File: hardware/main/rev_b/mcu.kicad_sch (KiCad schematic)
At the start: 23 parts, among them J10 SWD, U10 RP2354B, Y1 12MHz ABM8-272-T3

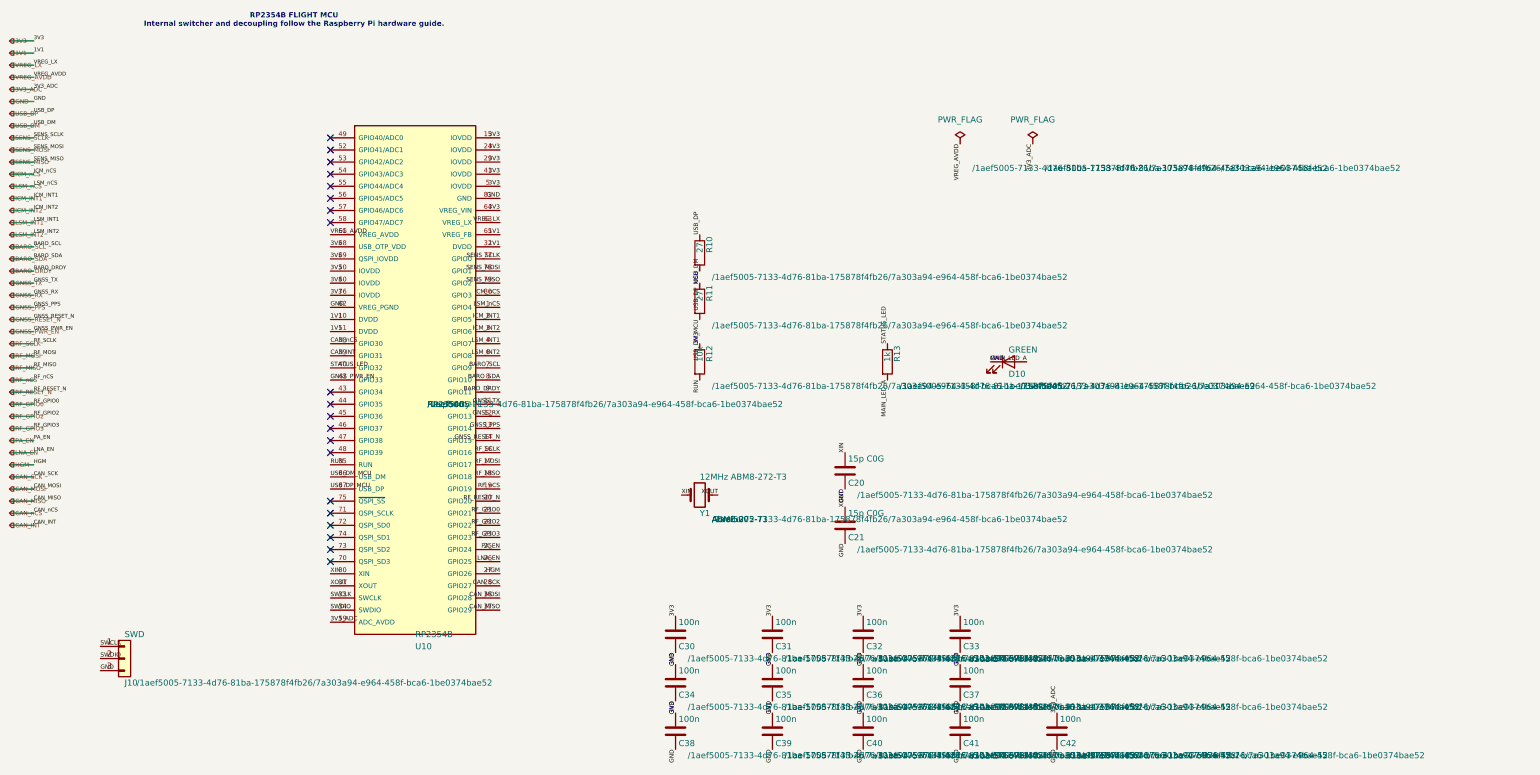
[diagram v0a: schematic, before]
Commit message: build: route and validate rev-b boards
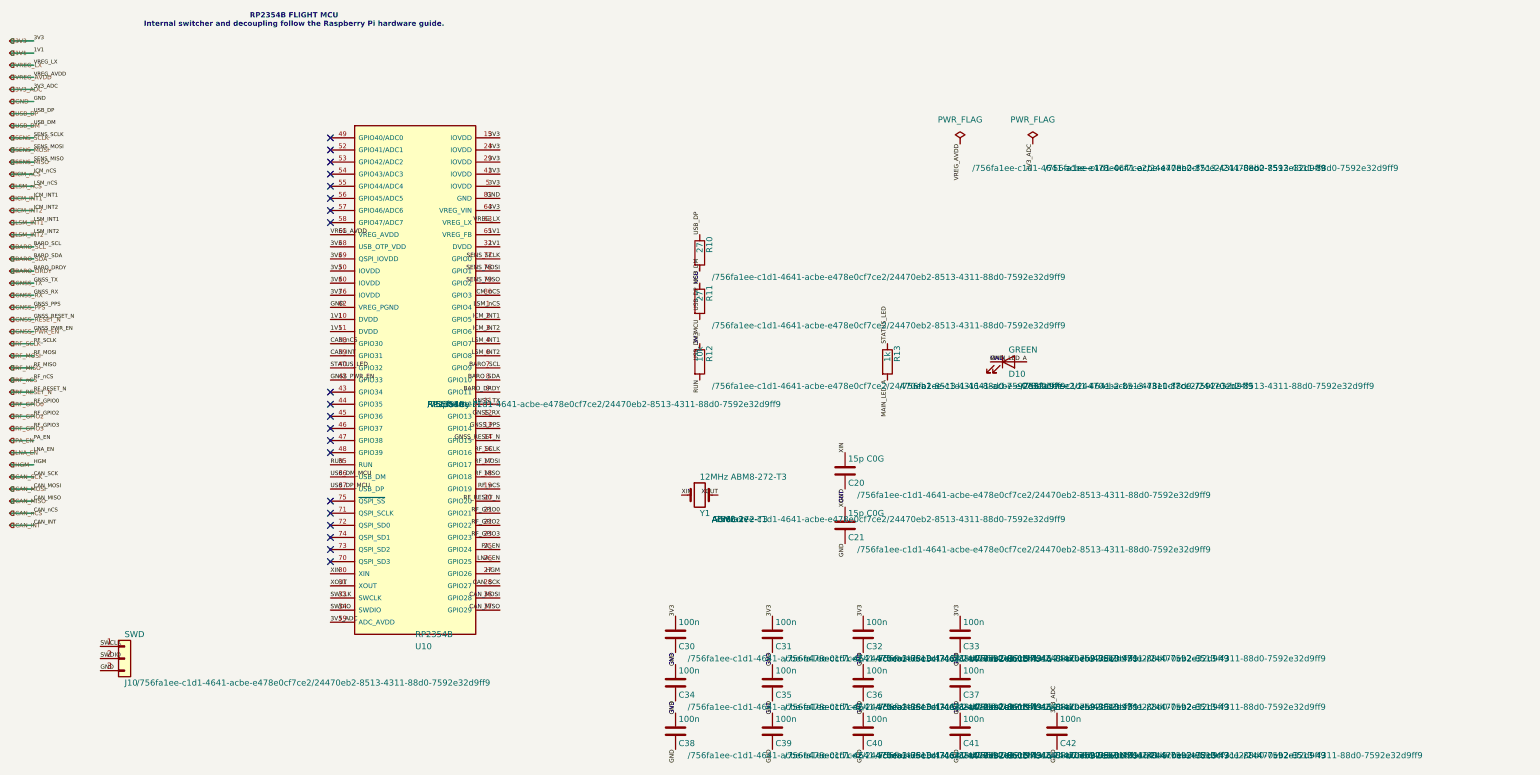
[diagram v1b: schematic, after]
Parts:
- C20, C21, C30, C31, C32, C33, C34, C35, C36, C37, C38, C39, C40, C41, C42, D10, J10, R10, R11, R12, R13, U10, Y1: hierarchy_path /1aef5005-7133-4d76-81ba-175878f4fb26/7a303a94-e964-458f-bc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 -> /756fa1ee-c1d1-4641-acbe-e478e0cf7ce2/24470eb2-8513-4311-88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

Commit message: build: route and validate rev-b boards
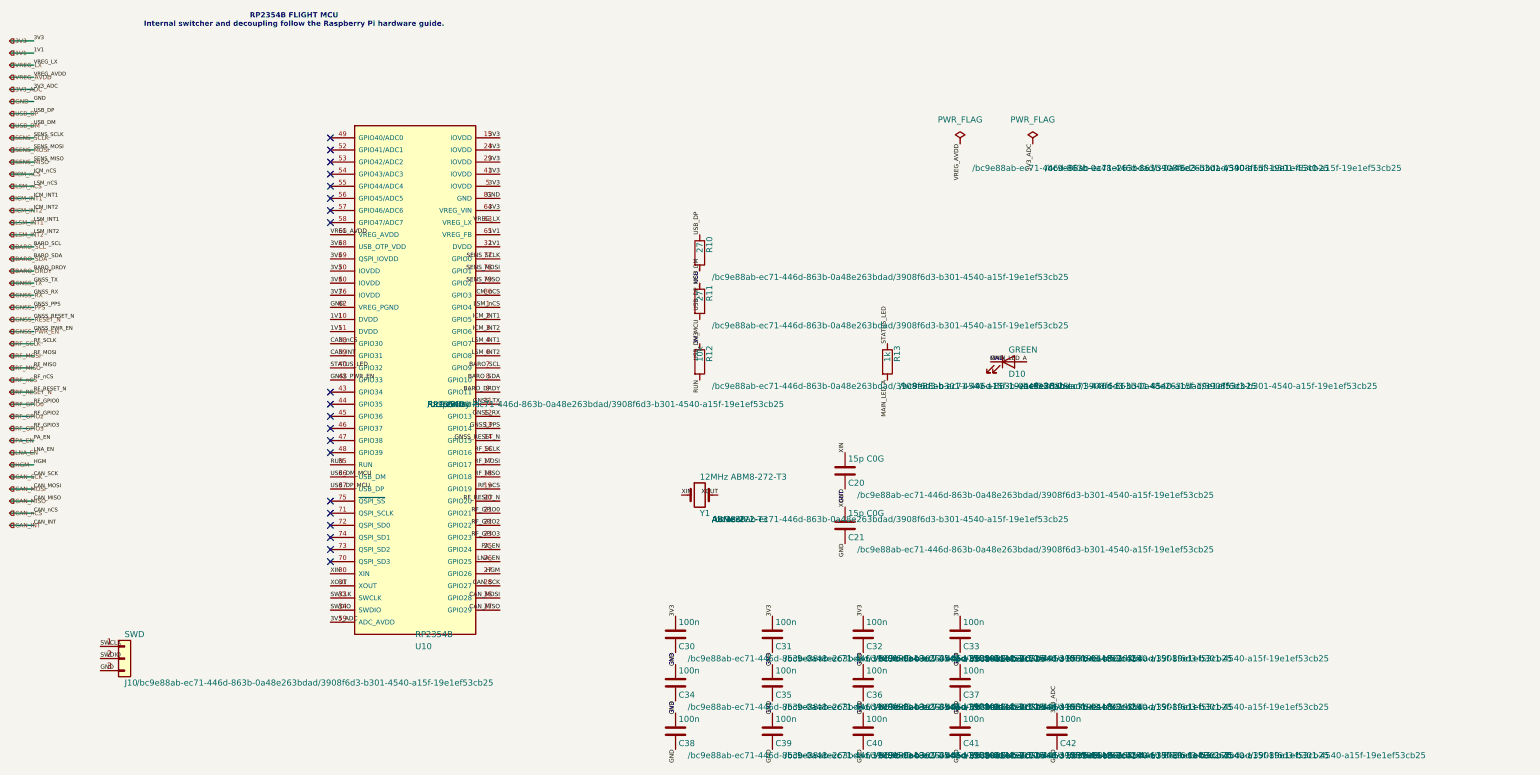
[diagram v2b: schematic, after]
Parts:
- C20, C21, C30, C31, C32, C33, C34, C35, C36, C37, C38, C39, C40, C41, C42, D10, J10, R10, R11, R12, R13, U10, Y1: hierarchy_path /756fa1ee-c1d1-4641-acbe-e478e0cf7ce2/24470eb2-8513-4311-88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 -> /bc9e88ab-ec71-446d-863b-0a48e263bdad/3908f6d3-b301-4540-a1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

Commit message: build: route and validate rev-b boards
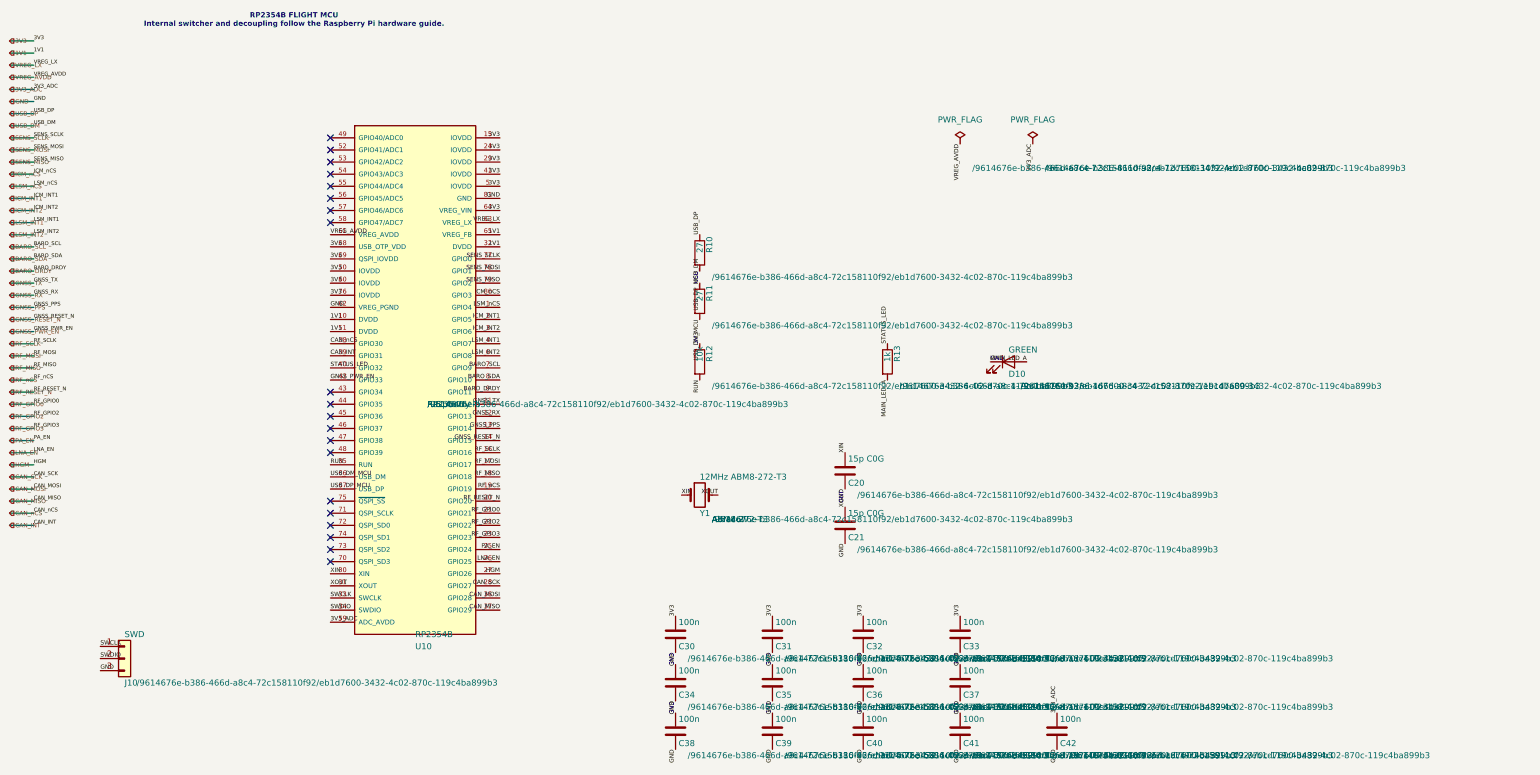
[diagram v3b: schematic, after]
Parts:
- C20, C21, C30, C31, C32, C33, C34, C35, C36, C37, C38, C39, C40, C41, C42, D10, J10, R10, R11, R12, R13, U10, Y1: hierarchy_path /bc9e88ab-ec71-446d-863b-0a48e263bdad/3908f6d3-b301-4540-a1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 -> /9614676e-b386-466d-a8c4-72c158110f92/eb1d7600-3432-4c02-87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
